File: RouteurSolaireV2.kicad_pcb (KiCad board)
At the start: 2 copper layers, 100 x 100 mm, 31 parts

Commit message: Version fonctionelle de PCB en cours de Dev.
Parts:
- added 100K: R_Axial_DIN0207_L6.3mm_D2.5mm_P10.16mm_Horizontal, Resistor_THT:R_Axial_DIN0207_L6.3mm_D2.5mm_P10.16mm_Horizontal, F.Cu at (64.1, 140.7)
- added 100K: R_Axial_DIN0207_L6.3mm_D2.5mm_P10.16mm_Horizontal, Resistor_THT:R_Axial_DIN0207_L6.3mm_D2.5mm_P10.16mm_Horizontal, F.Cu at (64.1, 126.7)
- added 4,7uF: CP_Radial_D5.0mm_P2.50mm, Capacitor_THT:CP_Radial_D5.0mm_P2.50mm, F.Cu at (58.2, 140.7)
- added GND / 10PWM: TerminalBlock_bornier-2_P5.08mm, TerminalBlock:TerminalBlock_bornier-2_P5.08mm, F.Cu at (75.5, 149.5)
- added GND / 11PWM: TerminalBlock_bornier-2_P5.08mm, TerminalBlock:TerminalBlock_bornier-2_P5.08mm, F.Cu at (98.0, 149.5)
- added R/Transfo: R_Axial_DIN0207_L6.3mm_D2.5mm_P10.16mm_Horizontal, Resistor_THT:R_Axial_DIN0207_L6.3mm_D2.5mm_P10.16mm_Horizontal, F.Cu at (68.6, 112.2)
- added R/Transfo: R_Axial_DIN0207_L6.3mm_D2.5mm_P10.16mm_Horizontal, Resistor_THT:R_Axial_DIN0207_L6.3mm_D2.5mm_P10.16mm_Horizontal, F.Cu at (68.6, 126.7)
- GND / 9PWM: renamed from REF**
- moved GND / 9PWM 88.1 mm to (87.0, 149.5), turned to 0 degrees
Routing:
- net (no net): track 1169.7 -> 1884.5 mm, vias 8 -> 13
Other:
- board text added: "24 A1"
- board text added: "25 A2"

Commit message: Version du fichier kicad conforme aux fichiers Gerber
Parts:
- removed PC817: DIP-4_W7.62mm, Package_DIP:DIP-4_W7.62mm
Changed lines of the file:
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@@
     (tracks 364)
     (zones 0)
-    (modules 38)
+    (modules 37)
     (nets 1)
   )
@@
     (pcbplotparams
       (layerselection 0x010fc_ffffffff)
-      (usegerberextensions false)
+      (usegerberextensions true)
       (usegerberattributes false)
       (usegerberadvancedattributes false)
@@
       (drillshape 0)
       (scaleselection 1)
-      (outputdirectory "/home/julien/Documents/Projets Kicad/legerber/"))
+      (outputdirectory "Gerber/"))
   )
   (net 0 "")
@@
       (at (xyz 0 0 0))
       (scale (xyz 1 1 1))
-      (rotate (xyz 0 0 0))
-    )
-  )
-  (module Package_DIP:DIP-4_W7.62mm (layer F.Cu)
-    (at 174 97.5)
-    (descr "4-lead though-hole mounted DIP package, row spacing 7.62 mm (300 mils)")
-    (tags "THT DIP DIL PDIP 2.54mm 7.62mm 300mil")
-    (fp_text reference PC817 (at 3.81 -2.33) (layer F.SilkS)
-      (effects (font (size 1 1) (thickness 0.15)))
-    )
-    (fp_text value DIP-4_W7.62mm (at 3.81 4.87) (layer F.Fab)
-      (effects (font (size 1 1) (thickness 0.15)))
-    )
-    (fp_text user %R (at 3.81 1.27) (layer F.Fab)
-      (effects (font (size 1 1) (thickness 0.15)))
-    )
-    (fp_line (start 8.7 -1.55) (end -1.1 -1.55) (layer F.CrtYd) (width 0.05))
-    (fp_line (start 8.7 4.1) (end 8.7 -1.55) (layer F.CrtYd) (width 0.05))
-    (fp_line (start -1.1 4.1) (end 8.7 4.1) (layer F.CrtYd) (width 0.05))
-    (fp_line (start -1.1 -1.55) (end -1.1 4.1) (layer F.CrtYd) (width 0.05))
-    (fp_line (start 6.46 -1.33) (end 4.81 -1.33) (layer F.SilkS) (width 0.12))
-    (fp_line (start 6.46 3.87) (end 6.46 -1.33) (layer F.SilkS) (width 0.12))
-    (fp_line (start 1.16 3.87) (end 6.46 3.87) (layer F.SilkS) (width 0.12))
-    (fp_line (start 1.16 -1.33) (end 1.16 3.87) (layer F.SilkS) (width 0.12))
-    (fp_line (start 2.81 -1.33) (end 1.16 -1.33) (layer F.SilkS) (width 0.12))
-    (fp_line (start 0.635 -0.27) (end 1.635 -1.27) (layer F.Fab) (width 0.1))
-    (fp_line (start 0.635 3.81) (end 0.635 -0.27) (layer F.Fab) (width 0.1))
-    (fp_line (start 6.985 3.81) (end 0.635 3.81) (layer F.Fab) (width 0.1))
-    (fp_line (start 6.985 -1.27) (end 6.985 3.81) (layer F.Fab) (width 0.1))
-    (fp_line (start 1.635 -1.27) (end 6.985 -1.27) (layer F.Fab) (width 0.1))
-    (fp_arc (start 3.81 -1.33) (end 2.81 -1.33) (angle -180) (layer F.SilkS) (width 0.12))
-    (pad 4 thru_hole oval (at 7.62 0) (size 1.6 1.6) (drill 0.8) (layers *.Cu *.Mask))
-    (pad 2 thru_hole oval (at 0 2.54) (size 1.6 1.6) (drill 0.8) (layers *.Cu *.Mask))
-    (pad 3 thru_hole oval (at 7.62 2.54) (size 1.6 1.6) (drill 0.8) (layers *.Cu *.Mask))
-    (pad 1 thru_hole rect (at 0 0) (size 1.6 1.6) (drill 0.8) (layers *.Cu *.Mask))
-    (model ${KISYS3DMOD}/Package_DIP.3dshapes/DIP-4_W7.62mm.wrl
-      (at (xyz 0 0 0))
-      (scale (xyz 1 1 1))

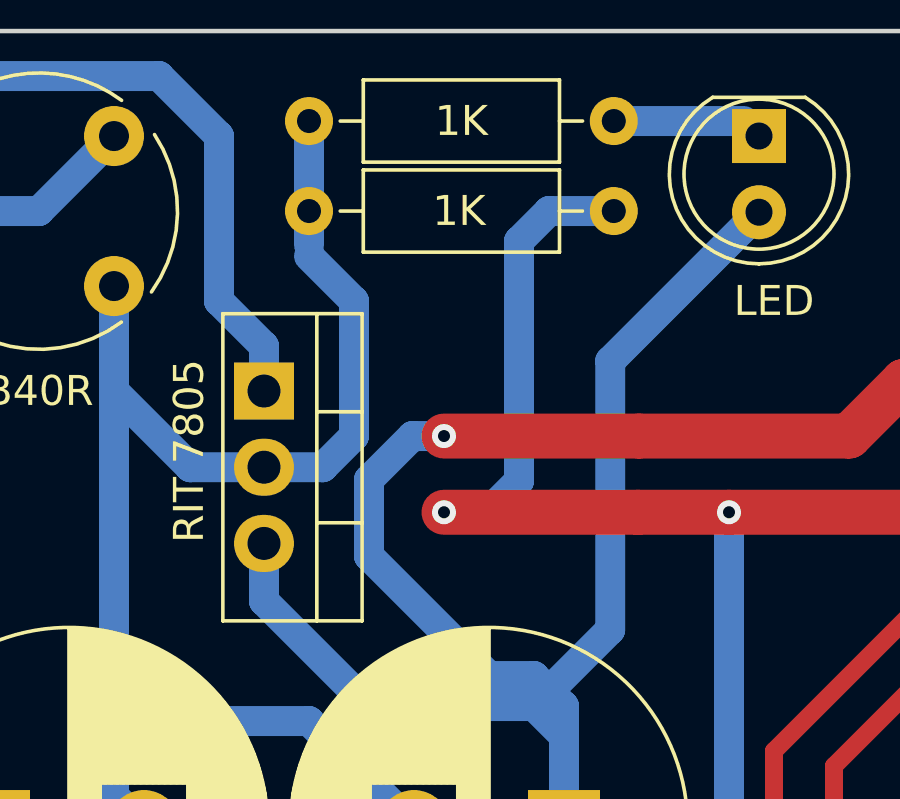
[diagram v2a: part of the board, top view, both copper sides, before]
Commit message: Correction valeur de résistance sur la couche silkS du fichier kicad et mise à jour du package zip
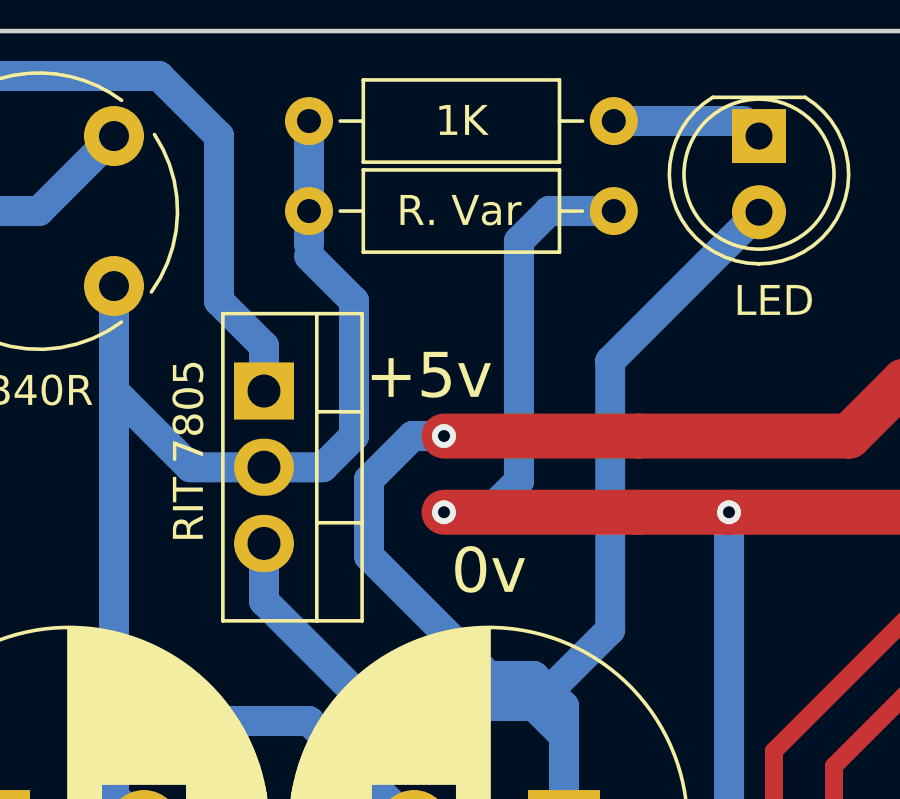
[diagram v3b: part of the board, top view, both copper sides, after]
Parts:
- R. Var: renamed from 1K
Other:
- board text added: "+5v"
- board text added: "0v"
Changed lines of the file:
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@@
   (general
     (thickness 1.6)
-    (drawings 8)
+    (drawings 10)
     (tracks 364)
     (zones 0)
@@
     (descr "Resistor, Axial_DIN0207 series, Axial, Horizontal, pin pitch=10.16mm, 0.25W = 1/4W, length*diameter=6.3*2.5mm^2, http://cdn-reichelt.de/documents/datenblatt/B400/1_4W%23YAG.pdf")
     (tags "Resistor Axial_DIN0207 series Axial Horizontal pin pitch 10.16mm 0.25W = 1/4W length 6.3mm diameter 2.5mm")
-    (fp_text reference 1K (at 5 0) (layer F.SilkS)
+    (fp_text reference "R. Var" (at 5 0) (layer F.SilkS)
       (effects (font (size 1 1) (thickness 0.15)))
     )
@@
       (rotate (xyz 0 0 0))
     )
+  )
+  (gr_text 0v (at 93.5 72.5) (layer F.SilkS)
+    (effects (font (size 1.5 1.5) (thickness 0.3)))
+  )
+  (gr_text +5v (at 91.5 66) (layer F.SilkS)
+    (effects (font (size 1.5 1.5) (thickness 0.3)))
   )
   (gr_text "25\nA2" (at 99 92) (layer F.SilkS)
@@
   (segment (start 40 72.5) (end 40 82.66) (width 3) (layer B.Cu) (net 0))
   (segment (start 92 68) (end 90.95 68) (width 1) (layer B.Cu) (net 0))
-  (via (at 92 68) (size 0.8) (drill 0.4) (layers F.Cu B.Cu) (net 0))
+  (via (at 92 68) (size 0.8) (drill 0.4) (layers F.Cu B.Cu) (net 0) (status 1000000))
   (segment (start 92 70.54) (end 92 70.54) (width 1) (layer B.Cu) (net 0))
   (via (at 92 70.54) (size 0.8) (drill 0.4) (layers F.Cu B.Cu) (net 0))

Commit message: Update code et PCB
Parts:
- added - LED +: TerminalBlock_bornier-2_P5.08mm, TerminalBlock:TerminalBlock_bornier-2_P5.08mm, F.Cu at (90.9, 109.9)
- added LDR720: TerminalBlock_bornier-2_P5.08mm, TerminalBlock:TerminalBlock_bornier-2_P5.08mm, F.Cu at (95.9, 134.9)
- added Link1: Pin_D0.7mm_L6.5mm_W1.8mm_FlatFork, Connector_Pin:Pin_D0.7mm_L6.5mm_W1.8mm_FlatFork, F.Cu at (126.0, 112.0)
- added Link1 Pin9: Pin_D0.7mm_L6.5mm_W1.8mm_FlatFork, Connector_Pin:Pin_D0.7mm_L6.5mm_W1.8mm_FlatFork, F.Cu at (103.0, 108.5)
- added Output var: TerminalBlock_bornier-2_P5.08mm, TerminalBlock:TerminalBlock_bornier-2_P5.08mm, F.Cu at (79.9, 134.9)
- added R 33k (LED): TerminalBlock_bornier-2_P5.08mm, TerminalBlock:TerminalBlock_bornier-2_P5.08mm, F.Cu at (84.9, 109.9)
- GND / D8: renamed from GND / 9PWM
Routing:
- net (no net): track 1884.5 -> 1971.0 mm, vias 13 -> 14
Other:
- board text added: "Routeur Solaire v3.0 Julien AMREIN - 2022"
- board text removed: "Routeur Solaire V2 Julien AMREIN - 2022"
